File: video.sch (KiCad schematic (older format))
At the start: 19 parts, among them CN9 DB23, U4 DENISE, U40 74LS245, U41 74LS245

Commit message: Add video power
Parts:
- added C4, C40, C41: 330n, symbol Device:C
- added C401, C402: 1000u, symbol Device:CP1
- added E406: 10n, symbol Device:EMI_Filter_LCL
- added unit 2 of HY1
- added R405: 0.47, Resistor_THT:R_Axial_DIN0309_L9.0mm_D3.2mm_P15.24mm_Horizontal, symbol Device:R
- added R406: 4.7, Resistor_THT:R_Axial_DIN0309_L9.0mm_D3.2mm_P15.24mm_Horizontal, symbol Device:R
- added unit 2 of U4
- added unit 2 of U40
- added unit 2 of U41
- R402, R403, R404: footprint (none) -> Raemixx500:R_Axial_DIN0309_L9.0mm_D3.2mm_P12.70mm_Horizontal
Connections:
- net labels added: VDDA
- wire segments 230 -> 278
- no-connect marks 4 -> 5
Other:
- note added: "+VXX = +12V supplied to video connector"
- note added: "1/2W"
- note added: "I'm pretty sure I've seen\n4.7 used here as well..."
- note added: "Note: Pin 2 and 21 of HY1\nconnected internally"
- note added: "TODO: Add color composite and S-Video,\nwith a new circuit based on the AD724 chip"
- note added: "VD (+VID\non original\nschematics) is\npicked up here"
- note added: "VDDA (+VXX\non original\nschematics) is\npicked up here"
- note added: "VIDEO POWER"
- note removed: "TODO: Add circuit that generates\ncolor composite and S-Video,\nbased on the AD724 chip"
- note removed: "TODO: Add power"

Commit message: Add power & decoupling, not yet complete
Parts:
- C401, C402: footprint (none) -> Capacitor_THT:CP_Radial_D8.0mm_P5.00mm
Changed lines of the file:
@@
 $Descr A3 16535 11693
 encoding utf-8
-Sheet 4 11
+Sheet 4 12
 Title "Rämixx500"
 Date "2019-04-14"
@@
 F 0 "C402" H 5265 8246 50  0000 L CNN
 F 1 "1000u" H 5265 8155 50  0000 L CNN
-F 2 "" H 5150 8200 50  0001 C CNN
+F 2 "Capacitor_THT:CP_Radial_D8.0mm_P5.00mm" H 5150 8200 50  0001 C CNN
 F 3 "~" H 5150 8200 50  0001 C CNN
 	1    5150 8200
@@
 F 0 "C401" H 9740 8246 50  0000 L CNN
 F 1 "1000u" H 9740 8155 50  0000 L CNN
-F 2 "" H 9625 8200 50  0001 C CNN
+F 2 "Capacitor_THT:CP_Radial_D8.0mm_P5.00mm" H 9625 8200 50  0001 C CNN
 F 3 "~" H 9625 8200 50  0001 C CNN
 	1    9625 8200

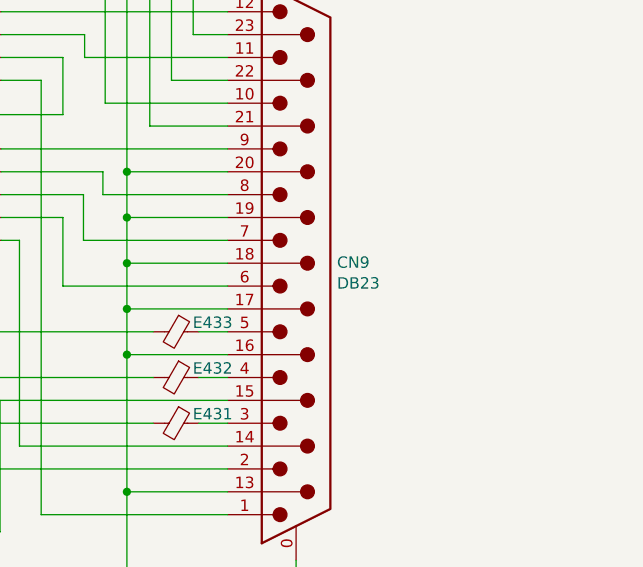
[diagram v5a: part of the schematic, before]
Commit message: Add external floppy connector (and do a few fixes)
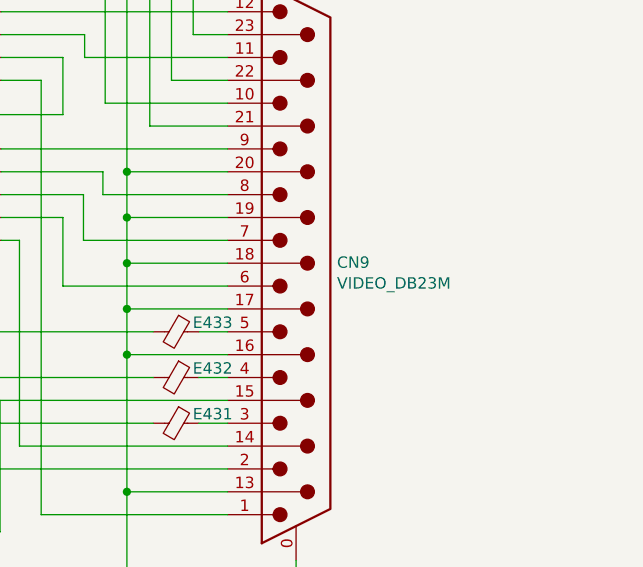
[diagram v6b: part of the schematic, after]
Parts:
- CN9: value DB23 -> VIDEO_DB23M
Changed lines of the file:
@@
 P 14680 4565
 F 0 "CN9" H 14859 4468 50  0000 L CNN
-F 1 "DB23" H 14859 4377 50  0000 L CNN
+F 1 "VIDEO_DB23M" H 14859 4377 50  0000 L CNN
 F 2 "" H 14680 4565 50  0001 C CNN
 F 3 " ~" H 14680 4565 50  0001 C CNN

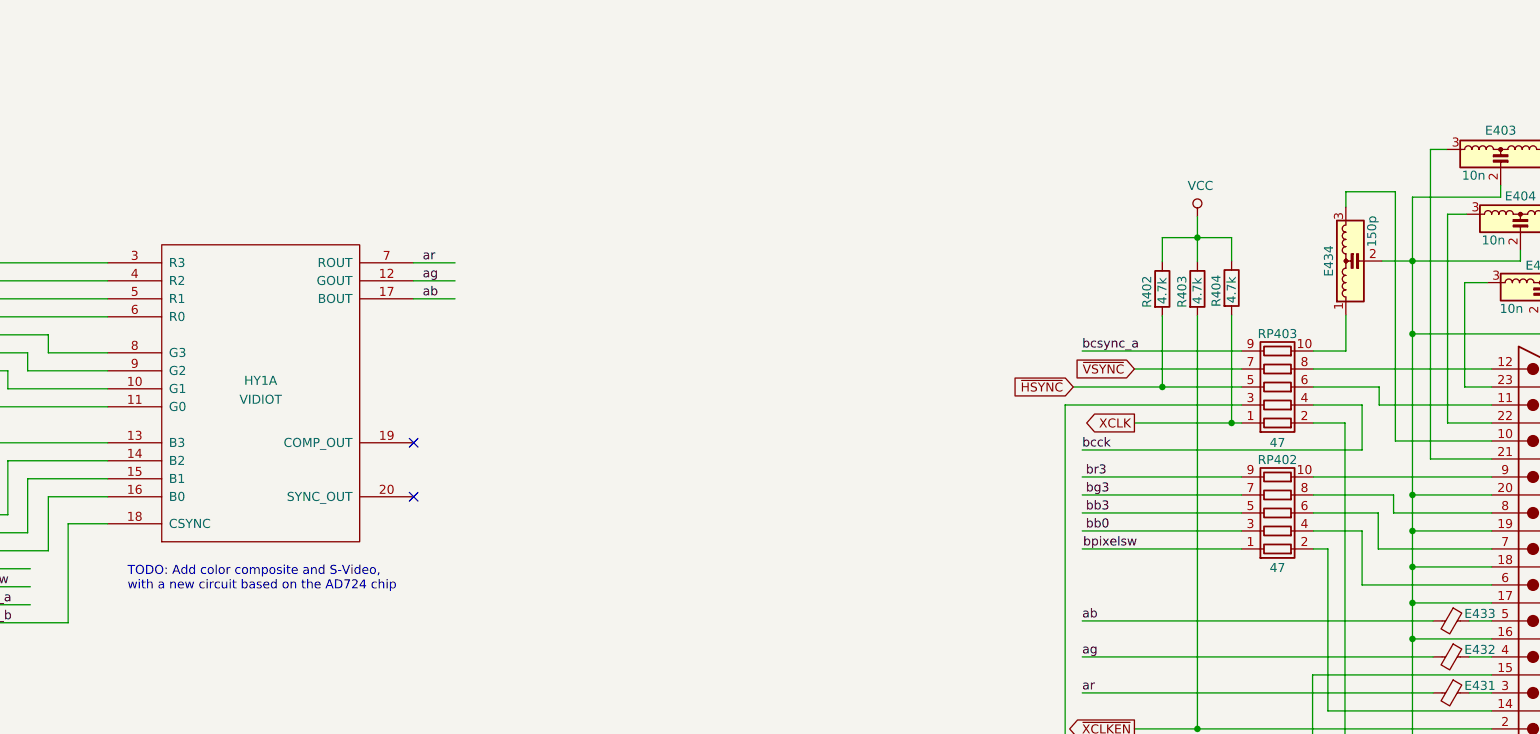
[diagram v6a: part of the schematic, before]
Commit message: Add composite output
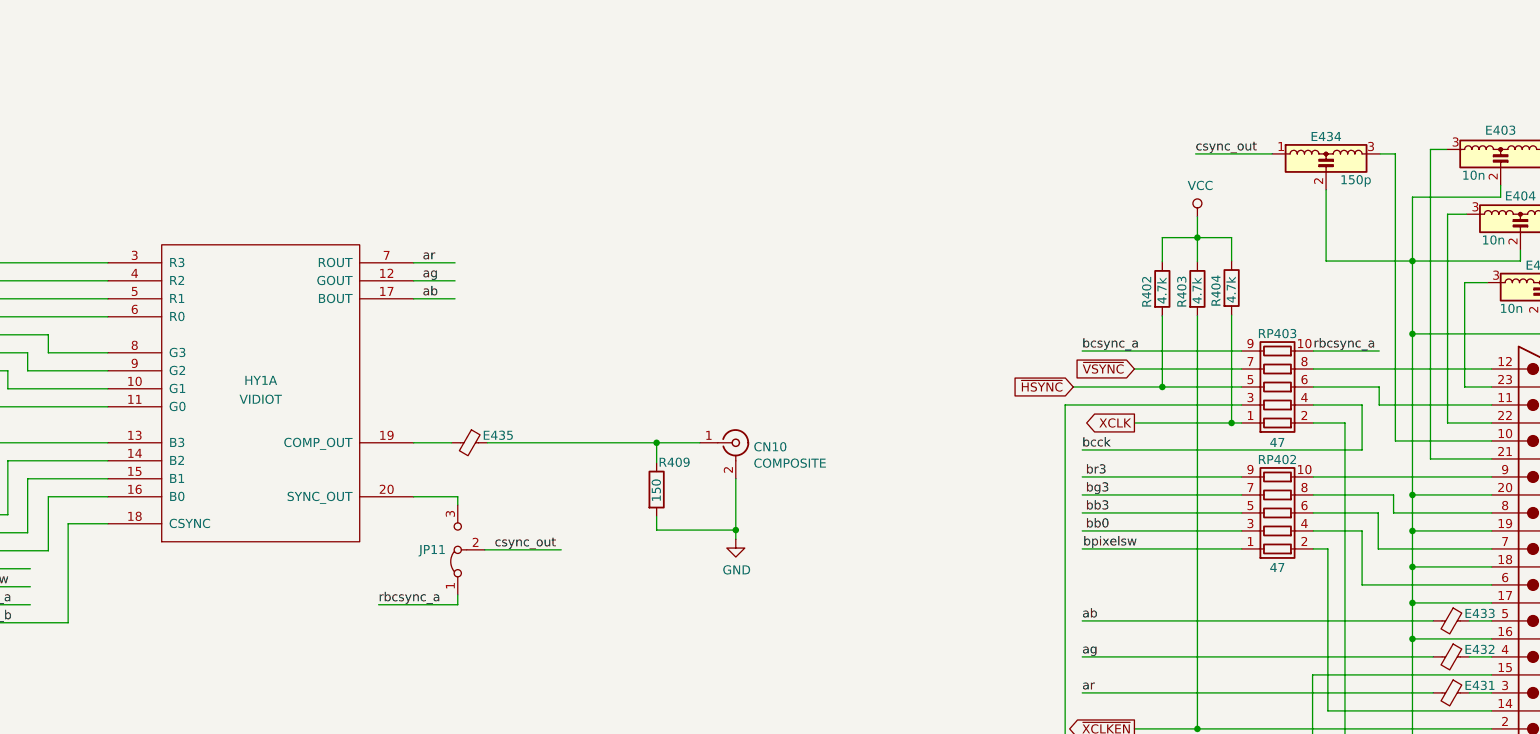
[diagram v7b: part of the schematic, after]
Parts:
- added CN10: COMPOSITE, w_conn_av:rca_yellow, symbol Connector:Conn_Coaxial
- added E435: Ferrite_Bead_Small, symbol Device:Ferrite_Bead_Small
- added JP11: Jumper_3_Bridged12, Raemixx500:Jumper3-Bridged12, symbol Jumper:Jumper_3_Bridged12
- added R409: 150, symbol Device:R
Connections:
- net labels added: csync_out, rbcsync_a
- wire segments 278 -> 291
- no-connect marks 5 -> 3
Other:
- note removed: "TODO: Add color composite and S-Video,\nwith a new circuit based on the AD724 chip"
- moved on the sheet: E434
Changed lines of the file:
@@
 	13940 4465 13940 4665
 Connection ~ 13940 4665
-NoConn ~ 8390 3975
-NoConn ~ 8390 4275
 $Comp
 L r_pack05:R_Pack05 RP402
@@
 Wire Wire Line
 	5830 4775 6260 4775
-Wire Wire Line
-	5830 4875 6260 4875
 Text Label 5840 4675 0    50   ~ 0
 bcck
@@
 L Device:EMI_Filter_LCL E434
 U 1 1 5D0EFA81
-P 13670 2965
-F 0 "E434" H 13670 3160 50  0000 C CNN
-F 1 "150p" H 13835 2920 50  0000 C CNN
-F 2 "" V 13670 2965 50  0001 C CNN
-F 3 "http://www.murata.com/~/media/webrenewal/support/library/catalog/products/emc/emifil/c31e.ashx?la=en-gb" V 13670 2965 50  0001 C CNN
-	1    13670 2965
-	0    -1   -1   0
-$EndComp
-Wire Wire Line
-	13390 3465 13570 3465
-Wire Wire Line
-	13570 3465 13570 3265
-Wire Wire Line
-	13770 2965 13940 2965
+P 13460 2470
+F 0 "E434" H 13460 2665 50  0000 C CNN
+F 1 "150p" H 13625 2425 50  0000 C CNN
+F 2 "" V 13460 2470 50  0001 C CNN
+F 3 "http://www.murata.com/~/media/webrenewal/support/library/catalog/products/emc/emifil/c31e.ashx?la=en-gb" V 13460 2470 50  0001 C CNN
+	1    13460 2470
+	1    0    0    -1
+$EndComp
 Wire Wire Line
 	13940 2965 13945 2965
 Wire Wire Line
-	13570 2665 13570 2580
-Wire Wire Line
-	13570 2580 13845 2580
-Wire Wire Line
-	13845 2580 13845 3965
+	13760 2370 13845 2370
+Wire Wire Line
+	13845 2370 13845 3965
 Wire Wire Line
 	13845 3965 14380 3965
@@
 Wire Wire Line
 	12745 2835 12745 2720
-Text Notes 6800 4800 0    50   ~ 0
-TODO: Add color composite and S-Video,\nwith a new circuit based on the AD724 chip
 Wire Wire Line
 	8390 2975 8620 2975
@@
 Text Notes 5120 9885 0    315  ~ 0
 VIDEO POWER
+$Comp
+L Jumper:Jumper_3_Bridged12 JP11
+U 1 1 5D80F9A3
+P 8635 4570
+F 0 "JP11" V 8635 4636 50  0000 L CNN
+F 1 "Jumper_3_Bridged12" V 8590 4636 50  0001 L CNN
+F 2 "Raemixx500:Jumper3-Bridged12" H 8635 4570 50  0001 C CNN
+F 3 "~" H 8635 4570 50  0001 C CNN
+	1    8635 4570
+	0    -1   -1   0
+$EndComp
+Wire Wire Line
+	8390 4275 8635 4275
+Wire Wire Line
+	8635 4275 8635 4320
+Wire Wire Line
+	8635 4875 8635 4820
+Wire Wire Line
+	8785 4570 9210 4570
+Text Label 8840 4570 0    50   ~ 0
+csync_out
+Wire Wire Line
+	13390 3465 13755 3465
+Wire Wire Line
+	5830 4875 6260 4875
+Wire Wire Line
+	8635 4875 8195 4875
+Text Label 8195 4875 0    50   ~ 0
+rbcsync_a
+Text Label 13390 3465 0    50   ~ 0
+rbcsync_a
+$Comp
+L Device:Ferrite_Bead_Small E435
+U 1 1 5D99AF23
+P 8700 3975
+F 0 "E435" V 8660 4135 50  0000 C CNN
+F 1 "Ferrite_Bead_Small" V 8554 3975 50  0001 C CNN
+F 2 "" V 8630 3975 50  0001 C CNN
+F 3 "~" H 8700 3975 50  0001 C CNN
+	1    8700 3975
+	0    1    1    0
+$EndComp
+$Comp
+L Connector:Conn_Coaxial CN?
+U 1 1 5D9B0BDD
+P 10180 3975
+AR Path="/5D2DC3A1/5D9B0BDD" Ref="CN?"  Part="1"
+AR Path="/5CBA5669/5D9B0BDD" Ref="CN10"  Part="1"
+F 0 "CN10" H 10279 3951 50  0000 L CNN
+F 1 "COMPOSITE" H 10279 3860 50  0000 L CNN
+F 2 "w_conn_av:rca_yellow" H 10180 3975 50  0001 C CNN
+F 3 " ~" H 10180 3975 50  0001 C CNN
+	1    10180 3975
+	1    0    0    -1
+$EndComp
+Wire Wire Line
+	8800 3975 9740 3975
+$Comp
+L power:GND #PWR0264
+U 1 1 5D9F0427
+P 10180 4510
+F 0 "#PWR0264" H 10180 4260 50  0001 C CNN
+F 1 "GND" H 10185 4337 50  0000 C CNN
+F 2 "" H 10180 4510 50  0001 C CNN
+F 3 "" H 10180 4510 50  0001 C CNN
+	1    10180 4510
+	1    0    0    -1
+$EndComp
+Wire Wire Line
+	10180 4510 10180 4460
+$Comp
+L Device:R R409
+U 1 1 5DA05B94
+P 9740 4235
+F 0 "R409" H 9750 4385 50  0000 L CNN
+F 1 "150" V 9740 4165 50  0000 L CNN
+F 2 "" V 9670 4235 50  0001 C CNN
+F 3 "~" H 9740 4235 50  0001 C CNN
+	1    9740 4235
+	1    0    0    -1
+$EndComp
+Wire Wire Line
+	9740 4385 9740 4460
+Wire Wire Line
+	9740 4460 10180 4460
+Connection ~ 10180 4460
+Wire Wire Line
+	10180 4460 10180 4175
+Wire Wire Line
+	9740 4085 9740 3975
+Connection ~ 9740 3975
+Wire Wire Line
+	9740 3975 9980 3975
+Text Label 12735 2370 0    50   ~ 0
+csync_out
+Wire Wire Line
+	12735 2370 13160 2370
+Wire Wire Line
+	13460 2570 13460 2965
+Wire Wire Line
+	13460 2965 13940 2965
+Wire Wire Line
+	8390 3975 8600 3975
 Wire Bus Line
 	2005 3775 2005 4475

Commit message: Fix power-up reset
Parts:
- C4, C40, C41: footprint (none) -> Raemixx500:C_Axial_L6.3mm_D2.5mm_P10.16mm
- CN9: footprint (none) -> Raemixx500:DB_23
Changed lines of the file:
@@
 EESchema Schematic File Version 4
 LIBS:Raemix500-cache
-EELAYER 26 0
+EELAYER 29 0
 EELAYER END
 $Descr A3 16535 11693
@@
 F 0 "CN9" H 14859 4468 50  0000 L CNN
 F 1 "VIDEO_DB23M" H 14859 4377 50  0000 L CNN
-F 2 "" H 14680 4565 50  0001 C CNN
+F 2 "Raemixx500:DB_23" H 14680 4565 50  0001 C CNN
 F 3 " ~" H 14680 4565 50  0001 C CNN
 	1    14680 4565
@@
 F 0 "C4" H 4365 8246 50  0000 L CNN
 F 1 "330n" H 4365 8155 50  0000 L CNN
-F 2 "" H 4288 8050 50  0001 C CNN
+F 2 "Raemixx500:C_Axial_L6.3mm_D2.5mm_P10.16mm" H 4288 8050 50  0001 C CNN
 F 3 "~" H 4250 8200 50  0001 C CNN
 	1    4250 8200
@@
 F 0 "C40" H 6865 8246 50  0000 L CNN
 F 1 "330n" H 6865 8155 50  0000 L CNN
-F 2 "" H 6788 8050 50  0001 C CNN
+F 2 "Raemixx500:C_Axial_L6.3mm_D2.5mm_P10.16mm" H 6788 8050 50  0001 C CNN
 F 3 "~" H 6750 8200 50  0001 C CNN
 	1    6750 8200
@@
 F 0 "C41" H 8315 8246 50  0000 L CNN
 F 1 "330n" H 8315 8155 50  0000 L CNN
-F 2 "" H 8238 8050 50  0001 C CNN
+F 2 "Raemixx500:C_Axial_L6.3mm_D2.5mm_P10.16mm" H 8238 8050 50  0001 C CNN
 F 3 "~" H 8200 8200 50  0001 C CNN
 	1    8200 8200
